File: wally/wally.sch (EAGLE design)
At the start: 102 parts, among them IC1 ESP32-S3-WROOM-1U-N16, IC2 XTLV61048DBVR, IC3 TLV1117LV33DCYR, IC4 DPS310XTSA1, IC6 LSM6DSV16BXTR, IC7 MLX90395KLW-BBA-001-SP, J1 MSD-4-A, J2 QWIIC_RIGHT_ANGLE, J3 QWIIC_RIGHT_ANGLE, J5 USB4105-GF-A, U1 RA-01H

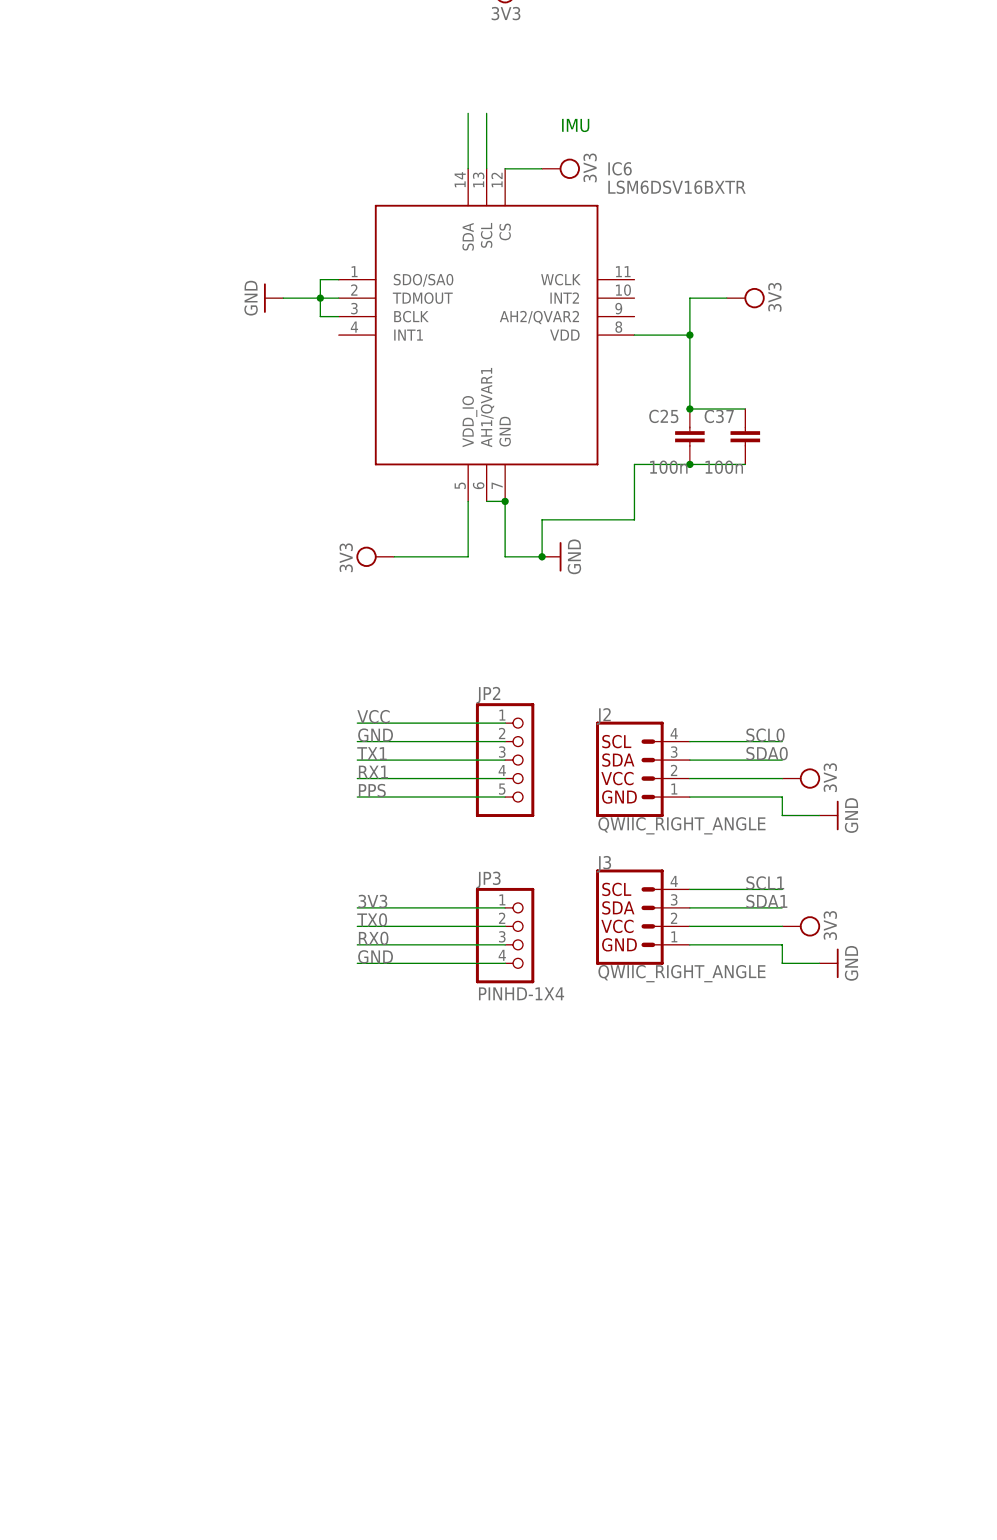
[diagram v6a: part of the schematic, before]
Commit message: add high range accel
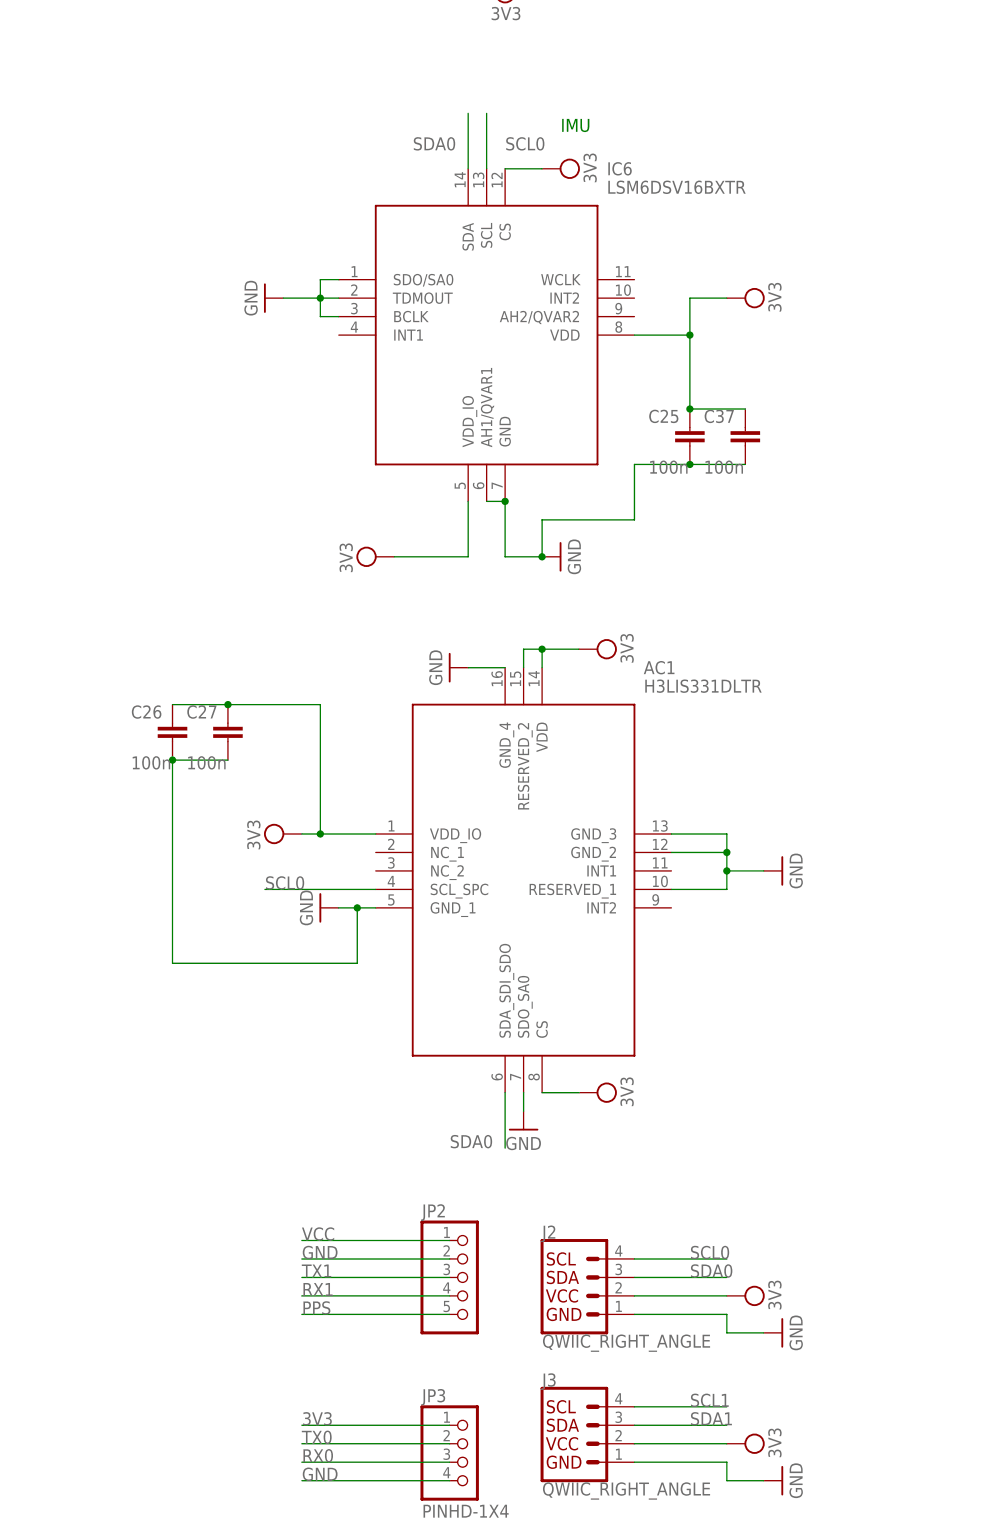
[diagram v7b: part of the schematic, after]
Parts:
- added AC1: H3LIS331DLTR, SamacSys_Parts:H3LIS331DLTR
- added C26, C27: 100n, Capacitor:C_CHIP-0402(1005-METRIC)
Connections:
- removed net N$5: IC6.SDA
- removed net N$6: IC6.SCL
- net 3V3: now also AC1.CS, AC1.RESERVED_2, AC1.VDD, AC1.VDD_IO, C26.1, C27.1
- net GND: now also AC1.GND_1, AC1.GND_2, AC1.GND_3, AC1.GND_4, AC1.RESERVED_1, AC1.SDO_SA0, C26.2, C27.2
- net SCL0: now also AC1.SCL_SPC, IC6.SCL
- net SDA0: now also AC1.SDA_SDI_SDO, IC6.SDA
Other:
- moved on the sheet: J2, J3, JP2, JP3

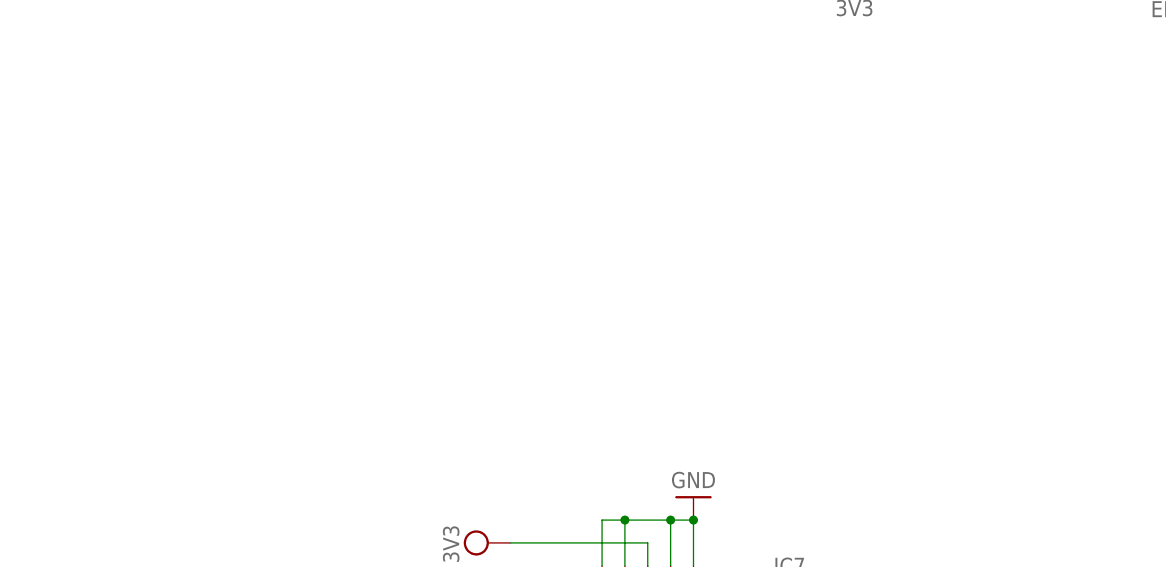
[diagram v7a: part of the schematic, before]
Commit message: add extended range baro
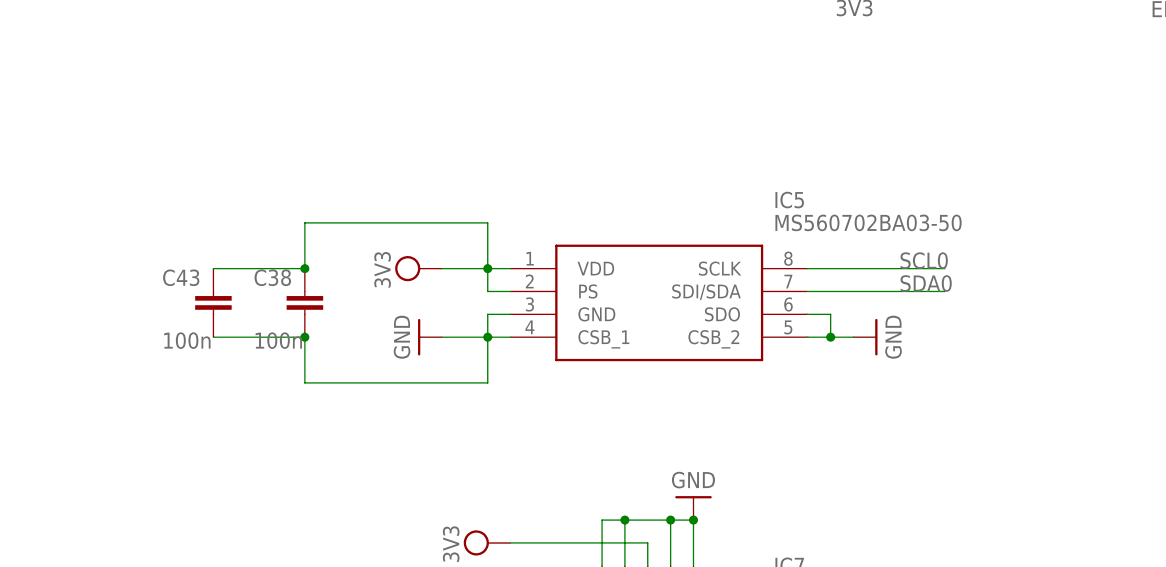
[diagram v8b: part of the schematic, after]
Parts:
- added C38, C43: 100n, Capacitor:C_CHIP-0402(1005-METRIC)
- added IC5: MS560702BA03-50, SamacSys_Parts:MS560702BA03-50
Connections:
- net 3V3: now also C38.1, C43.1, IC5.PS, IC5.VDD
- net GND: now also C38.2, C43.2, IC5.CSB_1, IC5.CSB_2, IC5.GND, IC5.SDO
- net SCL0: now also IC5.SCLK
- net SDA0: now also IC5.SDI/SDA
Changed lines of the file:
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@@
 <part name="C26" library="Capacitor" library_urn="urn:adsk.eagle:library:16290819" deviceset="C" device="CHIP-0402(1005-METRIC)" package3d_urn="urn:adsk.eagle:package:16290895/5" technology="_" value="100n"/>
 <part name="C27" library="Capacitor" library_urn="urn:adsk.eagle:library:16290819" deviceset="C" device="CHIP-0402(1005-METRIC)" package3d_urn="urn:adsk.eagle:package:16290895/5" technology="_" value="100n"/>
+<part name="IC5" library="SamacSys_Parts" deviceset="MS560702BA03-50" device=""/>
+<part name="SUPPLY51" library="Power_Symbols" library_urn="urn:adsk.eagle:library:16502351" deviceset="3V3-CIRCLE" device="" value="3V3"/>
+<part name="C38" library="Capacitor" library_urn="urn:adsk.eagle:library:16290819" deviceset="C" device="CHIP-0402(1005-METRIC)" package3d_urn="urn:adsk.eagle:package:16290895/5" technology="_" value="100n"/>
+<part name="SUPPLY52" library="Power_Symbols" library_urn="urn:adsk.eagle:library:16502351" deviceset="GND-BAR" device="" value="GND"/>
+<part name="SUPPLY53" library="Power_Symbols" library_urn="urn:adsk.eagle:library:16502351" deviceset="GND-BAR" device="" value="GND"/>
+<part name="C43" library="Capacitor" library_urn="urn:adsk.eagle:library:16290819" deviceset="C" device="CHIP-0402(1005-METRIC)" package3d_urn="urn:adsk.eagle:package:16290895/5" technology="_" value="100n"/>
 </parts>
 <sheets>
@@
 <attribute name="NAME" x="-31.115" y="-454.025" size="1.778" layer="95"/>
 <attribute name="VALUE" x="-31.115" y="-461.01" size="1.778" layer="96"/>
+</instance>
+<instance part="IC5" gate="G$1" x="-5.08" y="-264.16" smashed="yes">
+<attribute name="NAME" x="24.13" y="-256.54" size="1.778" layer="95" align="center-left"/>
+<attribute name="VALUE" x="24.13" y="-259.08" size="1.778" layer="96" align="center-left"/>
+</instance>
+<instance part="SUPPLY51" gate="G$1" x="-15.24" y="-264.16" smashed="yes" rot="R90">
+<attribute name="VALUE" x="-18.415" y="-264.287" size="1.778" layer="96" rot="R90" align="bottom-center"/>
+</instance>
+<instance part="C38" gate="G$1" x="-27.94" y="-266.7" smashed="yes">
+<attribute name="NAME" x="-33.655" y="-266.065" size="1.778" layer="95"/>
+<attribute name="VALUE" x="-33.655" y="-273.05" size="1.778" layer="96"/>
+</instance>
+<instance part="SUPPLY52" gate="G$1" x="-15.24" y="-271.78" smashed="yes" rot="R270">
+<attribute name="VALUE" x="-17.145" y="-271.78" size="1.778" layer="96" rot="R270" align="center"/>
+</instance>
+<instance part="SUPPLY53" gate="G$1" x="35.56" y="-271.78" smashed="yes" rot="R90">
+<attribute name="VALUE" x="37.465" y="-271.78" size="1.778" layer="96" rot="R90" align="center"/>
+</instance>
+<instance part="C43" gate="G$1" x="-38.1" y="-266.7" smashed="yes">
+<attribute name="NAME" x="-43.815" y="-266.065" size="1.778" layer="95"/>
+<attribute name="VALUE" x="-43.815" y="-273.05" size="1.778" layer="96"/>
 </instance>
 </instances>
@@
 <wire x1="7.62" y1="-447.04" x2="12.7" y2="-447.04" width="0.1524" layer="91"/>
 </segment>
+<segment>
+<pinref part="SUPPLY52" gate="G$1" pin="GND"/>
+<pinref part="IC5" gate="G$1" pin="CSB_1"/>
+<wire x1="-12.7" y1="-271.78" x2="-7.62" y2="-271.78" width="0.1524" layer="91"/>
+<pinref part="IC5" gate="G$1" pin="GND"/>
+<wire x1="-7.62" y1="-271.78" x2="-5.08" y2="-271.78" width="0.1524" layer="91"/>
+<wire x1="-5.08" y1="-269.24" x2="-7.62" y2="-269.24" width="0.1524" layer="91"/>
+<wire x1="-7.62" y1="-269.24" x2="-7.62" y2="-271.78" width="0.1524" layer="91"/>
+<junction x="-7.62" y="-271.78"/>
+<wire x1="-7.62" y1="-271.78" x2="-7.62" y2="-276.86" width="0.1524" layer="91"/>
+<wire x1="-7.62" y1="-276.86" x2="-27.94" y2="-276.86" width="0.1524" layer="91"/>
+<pinref part="C38" gate="G$1" pin="2"/>
+<wire x1="-27.94" y1="-276.86" x2="-27.94" y2="-271.78" width="0.1524" layer="91"/>
+<pinref part="C43" gate="G$1" pin="2"/>
+<wire x1="-38.1" y1="-271.78" x2="-27.94" y2="-271.78" width="0.1524" layer="91"/>
+<junction x="-27.94" y="-271.78"/>
+</segment>
+<segment>
+<pinref part="SUPPLY53" gate="G$1" pin="GND"/>
+<pinref part="IC5" gate="G$1" pin="CSB_2"/>
+<wire x1="33.02" y1="-271.78" x2="30.48" y2="-271.78" width="0.1524" layer="91"/>
+<pinref part="IC5" gate="G$1" pin="SDO"/>
+<wire x1="30.48" y1="-271.78" x2="27.94" y2="-271.78" width="0.1524" layer="91"/>
+<wire x1="27.94" y1="-269.24" x2="30.48" y2="-269.24" width="0.1524" layer="91"/>
+<wire x1="30.48" y1="-269.24" x2="30.48" y2="-271.78" width="0.1524" layer="91"/>
+<junction x="30.48" y="-271.78"/>
+</segment>
 </net>
 <net name="3V3" class="0">
@@
 <pinref part="AC1" gate="G$1" pin="CS"/>
 <wire x1="22.86" y1="-505.46" x2="17.78" y2="-505.46" width="0.1524" layer="91"/>
+</segment>
+<segment>
+<pinref part="SUPPLY51" gate="G$1" pin="3V3"/>
+<pinref part="IC5" gate="G$1" pin="VDD"/>
+<wire x1="-12.7" y1="-264.16" x2="-7.62" y2="-264.16" width="0.1524" layer="91"/>
+<pinref part="IC5" gate="G$1" pin="PS"/>
+<wire x1="-7.62" y1="-264.16" x2="-5.08" y2="-264.16" width="0.1524" layer="91"/>
+<wire x1="-5.08" y1="-266.7" x2="-7.62" y2="-266.7" width="0.1524" layer="91"/>
+<wire x1="-7.62" y1="-266.7" x2="-7.62" y2="-264.16" width="0.1524" layer="91"/>
+<junction x="-7.62" y="-264.16"/>
+<pinref part="C38" gate="G$1" pin="1"/>
+<wire x1="-27.94" y1="-264.16" x2="-27.94" y2="-259.08" width="0.1524" layer="91"/>
+<wire x1="-27.94" y1="-259.08" x2="-7.62" y2="-259.08" width="0.1524" layer="91"/>
+<wire x1="-7.62" y1="-259.08" x2="-7.62" y2="-264.16" width="0.1524" layer="91"/>
+<pinref part="C43" gate="G$1" pin="1"/>
+<wire x1="-38.1" y1="-264.16" x2="-27.94" y2="-264.16" width="0.1524" layer="91"/>
+<junction x="-27.94" y="-264.16"/>
 </segment>
 </net>
@@
 <label x="5.08" y="-513.08" size="1.778" layer="95"/>
 </segment>
+<segment>
+<pinref part="IC5" gate="G$1" pin="SDI/SDA"/>
+<wire x1="27.94" y1="-266.7" x2="43.18" y2="-266.7" width="0.1524" layer="91"/>
+<label x="38.1" y="-266.7" size="1.778" layer="95"/>
+</segment>
 </net>
 <net name="USB_P" class="0">
@@
 <label x="-20.32" y="-477.52" size="1.778" layer="95"/>
 </segment>
+<segment>
+<pinref part="IC5" gate="G$1" pin="SCLK"/>
+<wire x1="27.94" y1="-264.16" x2="43.18" y2="-264.16" width="0.1524" layer="91"/>
+<label x="38.1" y="-264.16" size="1.778" layer="95"/>
+</segment>
 </net>
